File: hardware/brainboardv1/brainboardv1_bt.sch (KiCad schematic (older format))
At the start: 7 parts

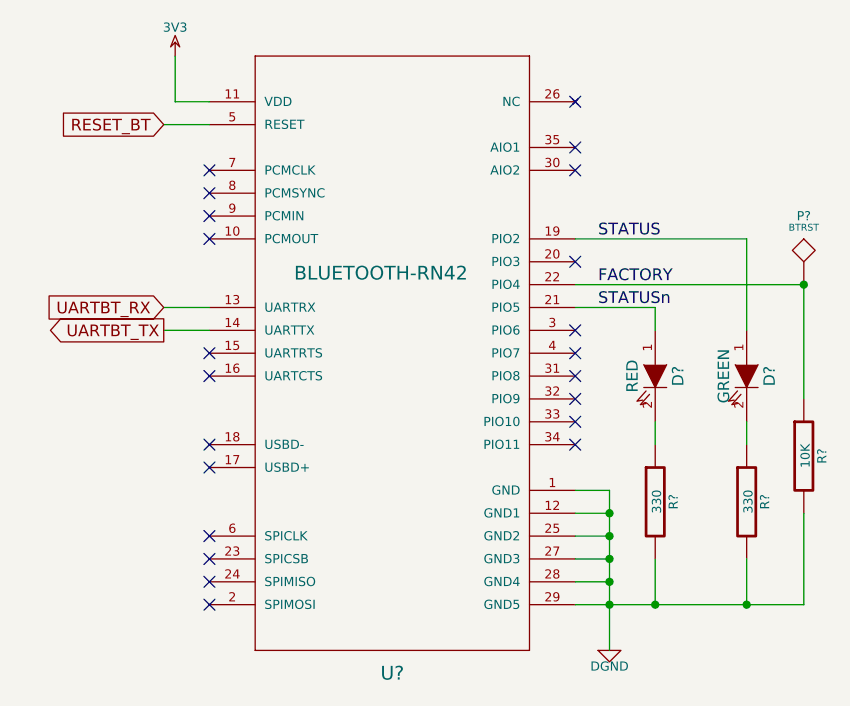
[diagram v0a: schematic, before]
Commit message: Nearly finished v1 sch & brd, await final check
Fixed errors from Rev 0, added MPU-6050 accelerometer/gyro for head
motion tracking, switched to +/-2.5V analog supply, added 2 bipolar
analog inputs for EOG tracking, added daisy-chain capability
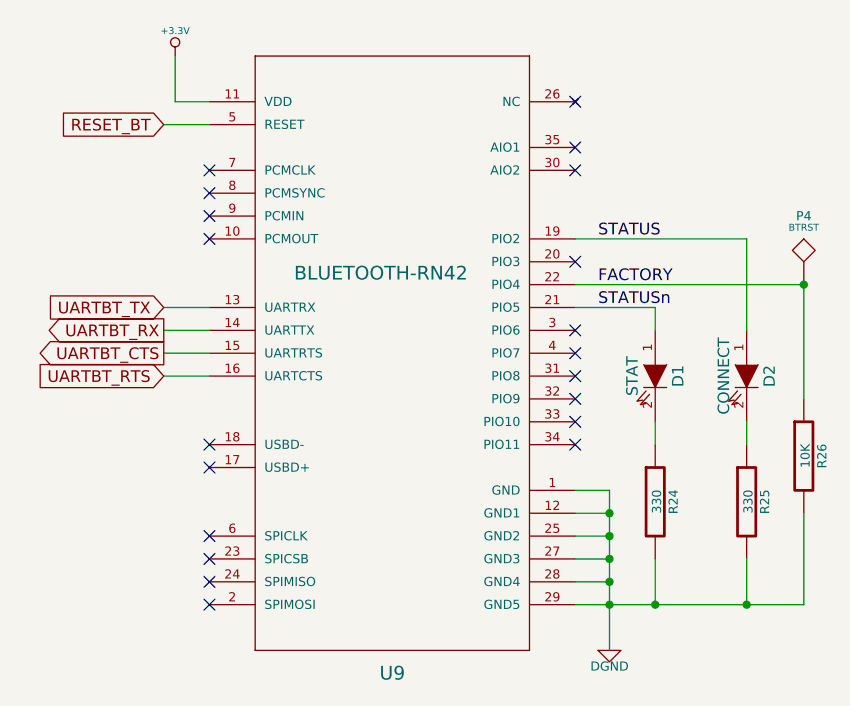
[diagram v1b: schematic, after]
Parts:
- D1: renamed from D?; value RED -> STAT
- D2: renamed from D?; value GREEN -> CONNECT
- gave numbers to parts that had none: 5
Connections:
- net UARTBT_RX: now also U9.14 (UARTTX); no longer U9.13 (UARTRX)
- net UARTBT_TX: now also U9.13 (UARTRX); no longer U9.14 (UARTTX)
- net UARTBT_CTS: now reaches U9.15 (UARTRTS)
- net UARTBT_RTS: now reaches U9.16 (UARTCTS)
- net 3V3 renamed +3.3V
- no-connect marks 22 -> 20
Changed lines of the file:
@@
 $Descr A4 11693 8268
 encoding utf-8
-Sheet 4 6
+Sheet 4 7
 Title "BrainBoard: Open-Source Hardware for Wearable BCI"
-Date "30 sep 2013"
+Date "27 dec 2013"
 Rev "0"
 Comp "Virginia Commonwealth University"
@@
 $EndDescr
 $Comp
-L BLUETOOTH-RN41" U?
+L BLUETOOTH-RN41" U9
 U 1 1 5244B495
 P 5650 3700
-F 0 "U?" H 5650 2300 60  0000 C CNN
+F 0 "U9" H 5650 2300 60  0000 C CNN
 F 1 "BLUETOOTH-RN42" H 5600 4050 60  0000 C CNN
 F 2 "" H 5650 3700 60  0000 C CNN
@@
 $EndComp
 $Comp
-L DGND #PWR?
+L DGND #PWR034
 U 1 1 5244B496
 P 6600 5000
-F 0 "#PWR?" H 6600 5000 40  0001 C CNN
+F 0 "#PWR034" H 6600 5000 40  0001 C CNN
 F 1 "DGND" H 6600 4930 40  0000 C CNN
 F 2 "" H 6600 5000 60  0000 C CNN
@@
 NoConn ~ 6450 4100
 $Comp
-L R R?
+L R R26
 U 1 1 5244B497
 P 7450 4150
-F 0 "R?" V 7530 4150 40  0000 C CNN
+F 0 "R26" V 7530 4150 40  0000 C CNN
 F 1 "10K" V 7457 4151 40  0000 C CNN
 F 2 "~" V 7380 4150 30  0000 C CNN
@@
 	7450 4800 7450 4400
 $Comp
-L TST P?
+L TST P4
 U 1 1 5244B498
 P 7450 3400
-F 0 "P?" H 7450 3700 40  0000 C CNN
+F 0 "P4" H 7450 3700 40  0000 C CNN
 F 1 "BTRST" H 7450 3650 30  0000 C CNN
 F 2 "~" H 7450 3400 60  0000 C CNN
@@
 Wire Wire Line
 	4850 3600 4650 3600
-NoConn ~ 4850 3700
-NoConn ~ 4850 3800
+Text GLabel 4650 3600 0    51   Output ~ 0
+UARTBT_RX
 Text GLabel 4650 3500 0    51   Input ~ 0
-UARTBT_RX
-Text GLabel 4650 3600 0    51   Output ~ 0
 UARTBT_TX
 Text GLabel 4650 2700 0    51   Input ~ 0
 RESET_BT
-$Comp
-L 3V3 #PWR?
-U 1 1 5244B499
-P 4700 2400
-F 0 "#PWR?" H 4700 2500 40  0001 C CNN
-F 1 "3V3" H 4700 2525 40  0000 C CNN
-F 2 "" H 4700 2400 60  0000 C CNN
-F 3 "" H 4700 2400 60  0000 C CNN
-	1    4700 2400
-	1    0    0    -1
-$EndComp
 NoConn ~ 4850 4500
 NoConn ~ 4850 4600
@@
 FACTORY
 $Comp
-L R R?
+L R R24
 U 1 1 5244B49A
 P 6800 4350
-F 0 "R?" V 6880 4350 40  0000 C CNN
+F 0 "R24" V 6880 4350 40  0000 C CNN
 F 1 "330" V 6807 4351 40  0000 C CNN
 F 2 "~" V 6730 4350 30  0000 C CNN
@@
 $EndComp
 $Comp
-L R R?
+L R R25
 U 1 1 5244B49B
 P 7200 4350
-F 0 "R?" V 7280 4350 40  0000 C CNN
+F 0 "R25" V 7280 4350 40  0000 C CNN
 F 1 "330" V 7207 4351 40  0000 C CNN
 F 2 "~" V 7130 4350 30  0000 C CNN
@@
 $EndComp
 $Comp
-L LED D?
+L LED D1
 U 1 1 5244B49C
 P 6800 3800
-F 0 "D?" H 6800 3900 50  0000 C CNN
-F 1 "RED" H 6800 3700 50  0000 C CNN
+F 0 "D1" H 6800 3900 50  0000 C CNN
+F 1 "STAT" H 6800 3700 50  0000 C CNN
 F 2 "~" H 6800 3800 60  0000 C CNN
 F 3 "~" H 6800 3800 60  0000 C CNN
@@
 $EndComp
 $Comp
-L LED D?
+L LED D2
 U 1 1 5244B49D
 P 7200 3800
-F 0 "D?" H 7200 3900 50  0000 C CNN
-F 1 "GREEN" H 7200 3700 50  0000 C CNN
+F 0 "D2" H 7200 3900 50  0000 C CNN
+F 1 "CONNECT" H 7200 3700 50  0000 C CNN
 F 2 "~" H 7200 3800 60  0000 C CNN
 F 3 "~" H 7200 3800 60  0000 C CNN
@@
 Text Label 6550 3500 0    51   ~ 0
 STATUSn
+$Comp
+L +3.3V #PWR035
+U 1 1 528FA0C8
+P 4700 2400
+F 0 "#PWR035" H 4700 2360 30  0001 C CNN
+F 1 "+3.3V" H 4700 2510 30  0000 C CNN
+F 2 "" H 4700 2400 60  0000 C CNN
+F 3 "" H 4700 2400 60  0000 C CNN
+	1    4700 2400
+	1    0    0    -1
+$EndComp
+Text GLabel 4650 3700 0    51   Output ~ 0
+UARTBT_CTS
+Text GLabel 4650 3800 0    51   Input ~ 0
+UARTBT_RTS
+Wire Wire Line
+	4650 3700 4850 3700
+Wire Wire Line
+	4650 3800 4850 3800
 $EndSCHEMATC
